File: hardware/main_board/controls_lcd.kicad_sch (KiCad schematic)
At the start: 28 parts, among them J3 2434804-1, Q1 AO3401A, Q3 AO3400A, Q4 AO3400A, Q5 AO3400A, SW3 SW_Push, U5 NHD-C0220BIZ-FSRGB

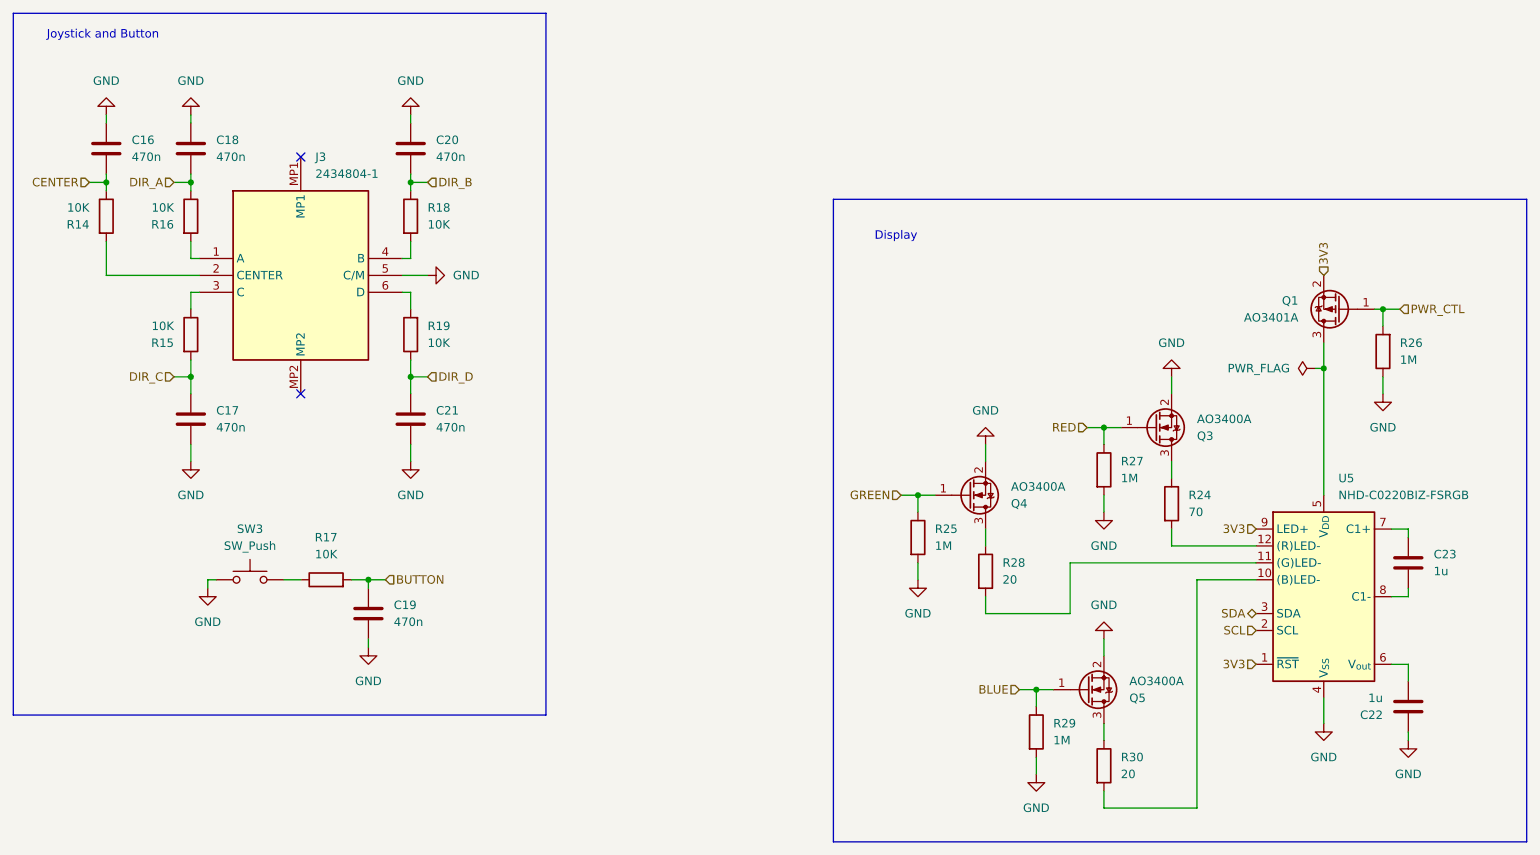
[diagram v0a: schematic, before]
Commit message: Add daughter board connector
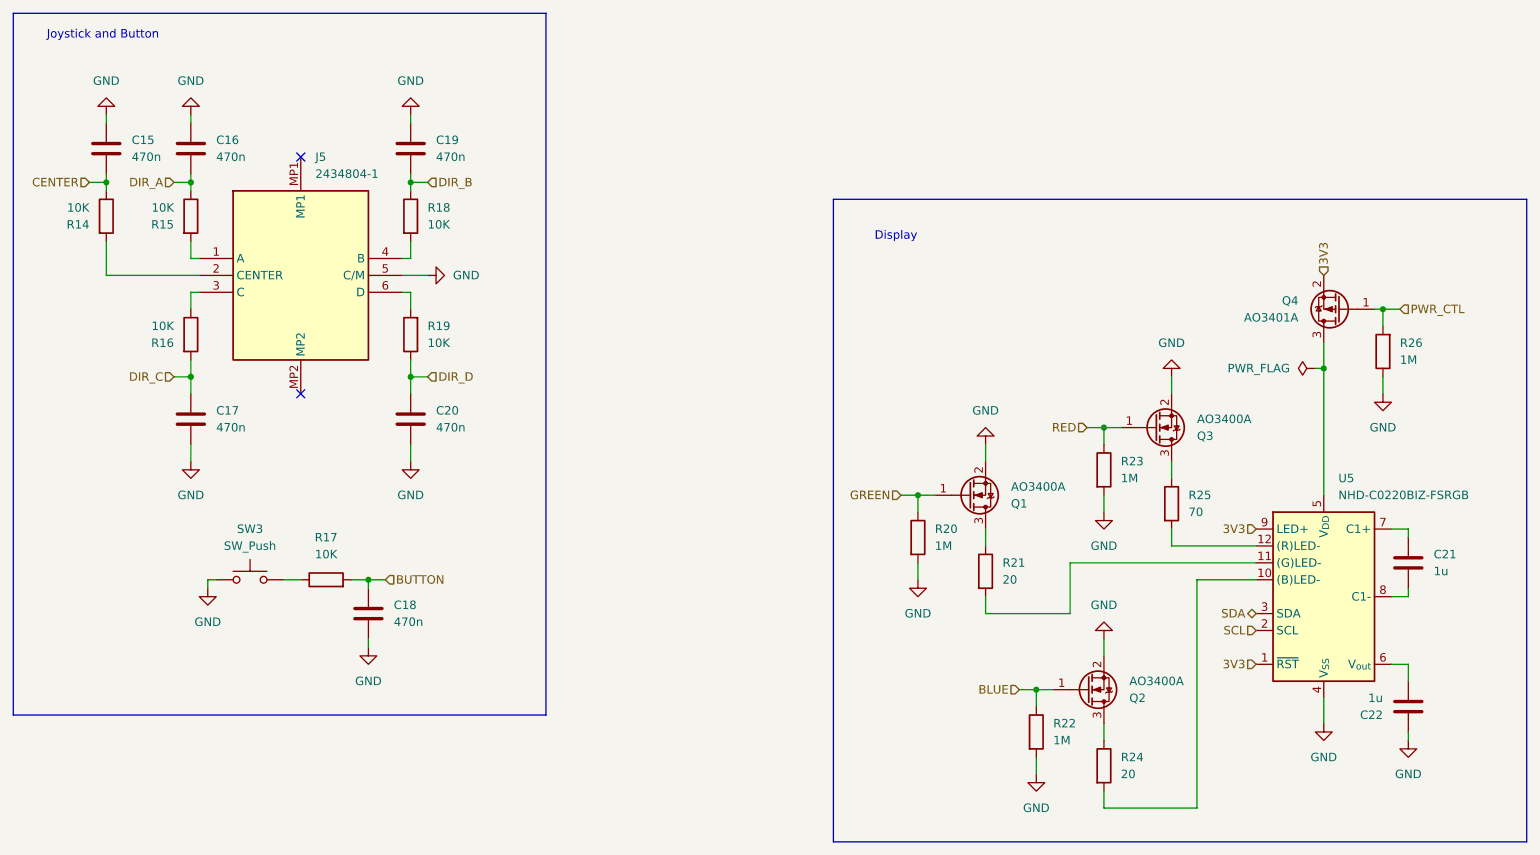
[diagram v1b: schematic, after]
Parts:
- J5: renamed from J3; footprint 24348041 -> Project_Footprints:TE_24348041
- renumbered C16 to C15, C18 to C16, C19 to C18, C20 to C19, C21 to C20, C23 to C21, Q4 to Q1, Q5 to Q2, Q1 to Q4, R16 to R15, R15 to R16, R25 to R20, R28 to R21, R29 to R22, R27 to R23, R30 to R24, R24 to R25

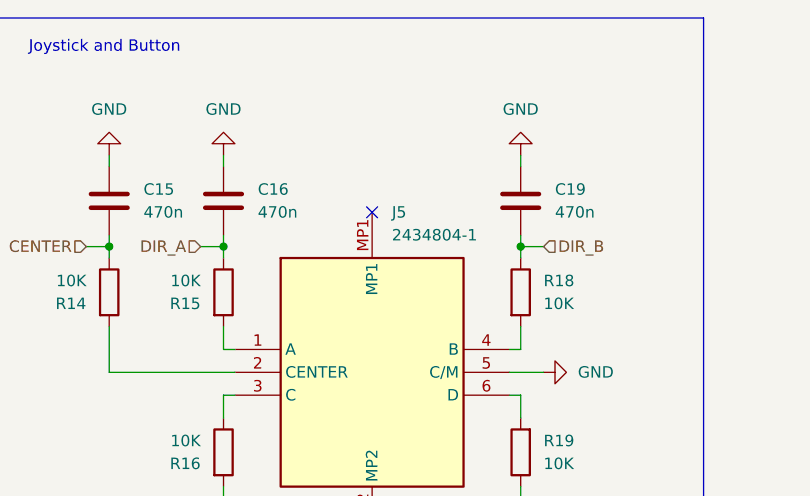
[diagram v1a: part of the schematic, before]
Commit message: Board schematic complete
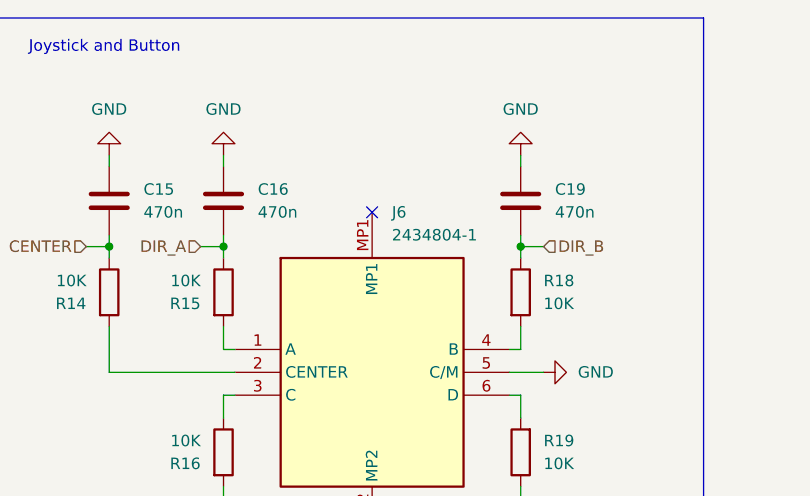
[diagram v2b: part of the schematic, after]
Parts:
- renumbered J5 to J6
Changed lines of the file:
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@@
 		(dnp no)
 		(fields_autoplaced yes)
-		(property "Reference" "#PWR033"
+		(property "Reference" "#PWR034"
 			(at 82.55 96.52 0)
 			(effects
@@
 			(project "main_board"
 				(path "/e7586151-38a0-41a9-9cce-542cfb7665db/8d2e8745-9bd7-47b1-9906-097dedd3973e"
-					(reference "#PWR033")
+					(reference "#PWR034")
 					(unit 1)
 				)
@@
 		(dnp no)
 		(fields_autoplaced yes)
-		(property "Reference" "#PWR037"
+		(property "Reference" "#PWR038"
 			(at 176.53 143.51 0)
 			(effects
@@
 			(project "main_board"
 				(path "/e7586151-38a0-41a9-9cce-542cfb7665db/8d2e8745-9bd7-47b1-9906-097dedd3973e"
-					(reference "#PWR037")
+					(reference "#PWR038")
 					(unit 1)
 				)
@@
 		(dnp no)
 		(fields_autoplaced yes)
-		(property "Reference" "#PWR043"
+		(property "Reference" "#PWR044"
 			(at 232.41 138.43 0)
 			(effects
@@
 			(project "main_board"
 				(path "/e7586151-38a0-41a9-9cce-542cfb7665db/8d2e8745-9bd7-47b1-9906-097dedd3973e"
-					(reference "#PWR043")
+					(reference "#PWR044")
 					(unit 1)
 				)
@@
 		(dnp no)
 		(fields_autoplaced yes)
-		(property "Reference" "#PWR040"
+		(property "Reference" "#PWR041"
 			(at 196.85 71.12 0)
 			(effects
@@
 			(project ""
 				(path "/e7586151-38a0-41a9-9cce-542cfb7665db/8d2e8745-9bd7-47b1-9906-097dedd3973e"
-					(reference "#PWR040")
+					(reference "#PWR041")
 					(unit 1)
 				)
@@
 		(dnp no)
 		(fields_autoplaced yes)
-		(property "Reference" "#PWR030"
+		(property "Reference" "#PWR031"
 			(at 52.07 115.57 0)
 			(effects
@@
 			(project "main_board"
 				(path "/e7586151-38a0-41a9-9cce-542cfb7665db/8d2e8745-9bd7-47b1-9906-097dedd3973e"
-					(reference "#PWR030")
+					(reference "#PWR031")
 					(unit 1)
 				)
@@
 		(dnp no)
 		(fields_autoplaced yes)
-		(property "Reference" "#PWR032"
+		(property "Reference" "#PWR033"
 			(at 82.55 31.75 0)
 			(effects
@@
 			(project ""
 				(path "/e7586151-38a0-41a9-9cce-542cfb7665db/8d2e8745-9bd7-47b1-9906-097dedd3973e"
-					(reference "#PWR032")
+					(reference "#PWR033")
 					(unit 1)
 				)
@@
 		(dnp no)
 		(fields_autoplaced yes)
-		(property "Reference" "#PWR035"
+		(property "Reference" "#PWR036"
 			(at 158.75 114.3 0)
 			(effects
@@
 			(project "main_board"
 				(path "/e7586151-38a0-41a9-9cce-542cfb7665db/8d2e8745-9bd7-47b1-9906-097dedd3973e"
-					(reference "#PWR035")
+					(reference "#PWR036")
 					(unit 1)
 				)
@@
 		(dnp no)
 		(fields_autoplaced yes)
-		(property "Reference" "#PWR039"
+		(property "Reference" "#PWR040"
 			(at 186.69 110.49 0)
 			(effects
@@
 			(project "main_board"
 				(path "/e7586151-38a0-41a9-9cce-542cfb7665db/8d2e8745-9bd7-47b1-9906-097dedd3973e"
-					(reference "#PWR039")
+					(reference "#PWR040")
 					(unit 1)
 				)
@@
 		(dnp no)
 		(fields_autoplaced yes)
-		(property "Reference" "#PWR042"
+		(property "Reference" "#PWR043"
 			(at 228.6 86.36 0)
 			(effects
@@
 			(project ""
 				(path "/e7586151-38a0-41a9-9cce-542cfb7665db/8d2e8745-9bd7-47b1-9906-097dedd3973e"
-					(reference "#PWR042")
+					(reference "#PWR043")
 					(unit 1)
 				)
@@
 		(dnp no)
 		(fields_autoplaced yes)
-		(property "Reference" "#PWR034"
+		(property "Reference" "#PWR035"
 			(at 91.44 62.23 0)
 			(effects
@@
 			(project "main_board"
 				(path "/e7586151-38a0-41a9-9cce-542cfb7665db/8d2e8745-9bd7-47b1-9906-097dedd3973e"
-					(reference "#PWR034")
+					(reference "#PWR035")
 					(unit 1)
 				)
@@
 		(dnp no)
 		(fields_autoplaced yes)
-		(property "Reference" "#PWR038"
+		(property "Reference" "#PWR039"
 			(at 186.69 104.14 0)
 			(effects
@@
 			(project ""
 				(path "/e7586151-38a0-41a9-9cce-542cfb7665db/8d2e8745-9bd7-47b1-9906-097dedd3973e"
-					(reference "#PWR038")
+					(reference "#PWR039")
 					(unit 1)
 				)
@@
 		(dnp no)
 		(fields_autoplaced yes)
-		(property "Reference" "#PWR027"
+		(property "Reference" "#PWR028"
 			(at 36.83 31.75 0)
 			(effects
@@
 			(project "main_board"
 				(path "/e7586151-38a0-41a9-9cce-542cfb7665db/8d2e8745-9bd7-47b1-9906-097dedd3973e"
-					(reference "#PWR027")
+					(reference "#PWR028")
 					(unit 1)
 				)
@@
 		(dnp no)
 		(fields_autoplaced yes)
-		(property "Reference" "#PWR028"
+		(property "Reference" "#PWR029"
 			(at 49.53 31.75 0)
 			(effects
@@
 			(project "main_board"
 				(path "/e7586151-38a0-41a9-9cce-542cfb7665db/8d2e8745-9bd7-47b1-9906-097dedd3973e"
-					(reference "#PWR028")
+					(reference "#PWR029")
 					(unit 1)
 				)
@@
 		(dnp no)
 		(fields_autoplaced yes)
-		(property "Reference" "J5"
+		(property "Reference" "J6"
 			(at 68.2341 44.45 0)
 			(effects
@@
 			(project ""
 				(path "/e7586151-38a0-41a9-9cce-542cfb7665db/8d2e8745-9bd7-47b1-9906-097dedd3973e"
-					(reference "J5")
+					(reference "J6")
 					(unit 1)
 				)
@@
 		(dnp no)
 		(fields_autoplaced yes)
-		(property "Reference" "#FLG03"
+		(property "Reference" "#FLG04"
 			(at 216.535 76.2 0)
 			(effects
@@
 			(project ""
 				(path "/e7586151-38a0-41a9-9cce-542cfb7665db/8d2e8745-9bd7-47b1-9906-097dedd3973e"
-					(reference "#FLG03")
+					(reference "#FLG04")
 					(unit 1)
 				)
@@
 		(dnp no)
 		(fields_autoplaced yes)
-		(property "Reference" "#PWR041"
+		(property "Reference" "#PWR042"
 			(at 219.71 135.89 0)
 			(effects
@@
 			(project "main_board"
 				(path "/e7586151-38a0-41a9-9cce-542cfb7665db/8d2e8745-9bd7-47b1-9906-097dedd3973e"
-					(reference "#PWR041")
+					(reference "#PWR042")
 					(unit 1)
 				)
@@
 		(dnp no)
 		(fields_autoplaced yes)
-		(property "Reference" "#PWR031"
+		(property "Reference" "#PWR032"
 			(at 76.2 124.46 0)
 			(effects
@@
 			(project "main_board"
 				(path "/e7586151-38a0-41a9-9cce-542cfb7665db/8d2e8745-9bd7-47b1-9906-097dedd3973e"
-					(reference "#PWR031")
+					(reference "#PWR032")
 					(unit 1)
 				)
@@
 		(dnp no)
 		(fields_autoplaced yes)
-		(property "Reference" "#PWR036"
+		(property "Reference" "#PWR037"
 			(at 168.91 81.28 0)
 			(effects
@@
 			(project "main_board"
 				(path "/e7586151-38a0-41a9-9cce-542cfb7665db/8d2e8745-9bd7-47b1-9906-097dedd3973e"
-					(reference "#PWR036")
+					(reference "#PWR037")
 					(unit 1)
 				)
@@
 		(dnp no)
 		(fields_autoplaced yes)
-		(property "Reference" "#PWR029"
+		(property "Reference" "#PWR030"
 			(at 49.53 96.52 0)
 			(effects
@@
 			(project "main_board"
 				(path "/e7586151-38a0-41a9-9cce-542cfb7665db/8d2e8745-9bd7-47b1-9906-097dedd3973e"
-					(reference "#PWR029")
+					(reference "#PWR030")
 					(unit 1)
 				)

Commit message: Routed mainboard PCB
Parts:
- R20, R22, R23: footprint (none) -> Resistor_SMD:R_0402_1005Metric
- U5: footprint Display:NHD-C0220BiZ-FSRGB -> Project_Footprints:NHD-C0220BiZ-FSRGB_no_mount
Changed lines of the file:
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@@
 			)
 		)
-		(property "Footprint" ""
+		(property "Footprint" "Resistor_SMD:R_0402_1005Metric"
 			(at 184.912 91.44 90)
 			(effects
@@
 		(dnp no)
 		(fields_autoplaced yes)
-		(property "Reference" "#PWR034"
+		(property "Reference" "#PWR35"
 			(at 82.55 96.52 0)
 			(effects
@@
 			(project "main_board"
 				(path "/e7586151-38a0-41a9-9cce-542cfb7665db/8d2e8745-9bd7-47b1-9906-097dedd3973e"
-					(reference "#PWR034")
+					(reference "#PWR35")
 					(unit 1)
 				)
@@
 		(dnp no)
 		(fields_autoplaced yes)
-		(property "Reference" "#PWR038"
+		(property "Reference" "#PWR39"
 			(at 176.53 143.51 0)
 			(effects
@@
 			(project "main_board"
 				(path "/e7586151-38a0-41a9-9cce-542cfb7665db/8d2e8745-9bd7-47b1-9906-097dedd3973e"
-					(reference "#PWR038")
+					(reference "#PWR39")
 					(unit 1)
 				)
@@
 		(dnp no)
 		(fields_autoplaced yes)
-		(property "Reference" "#PWR044"
+		(property "Reference" "#PWR45"
 			(at 232.41 138.43 0)
 			(effects
@@
 			(project "main_board"
 				(path "/e7586151-38a0-41a9-9cce-542cfb7665db/8d2e8745-9bd7-47b1-9906-097dedd3973e"
-					(reference "#PWR044")
+					(reference "#PWR45")
 					(unit 1)
 				)
@@
 			)
 		)
-		(property "Footprint" "Display:NHD-C0220BiZ-FSRGB"
+		(property "Footprint" "Project_Footprints:NHD-C0220BiZ-FSRGB_no_mount"
 			(at 219.71 113.03 0)
 			(effects
@@
 		(dnp no)
 		(fields_autoplaced yes)
-		(property "Reference" "#PWR041"
+		(property "Reference" "#PWR42"
 			(at 196.85 71.12 0)
 			(effects
@@
 			(project ""
 				(path "/e7586151-38a0-41a9-9cce-542cfb7665db/8d2e8745-9bd7-47b1-9906-097dedd3973e"
-					(reference "#PWR041")
+					(reference "#PWR42")
 					(unit 1)
 				)
@@
 			)
 		)
-		(property "Footprint" ""
+		(property "Footprint" "Resistor_SMD:R_0402_1005Metric"
 			(at 174.752 130.81 90)
 			(effects
@@
 		(dnp no)
 		(fields_autoplaced yes)
-		(property "Reference" "#PWR031"
+		(property "Reference" "#PWR32"
 			(at 52.07 115.57 0)
 			(effects
@@
 			(project "main_board"
 				(path "/e7586151-38a0-41a9-9cce-542cfb7665db/8d2e8745-9bd7-47b1-9906-097dedd3973e"
-					(reference "#PWR031")
+					(reference "#PWR32")
 					(unit 1)
 				)
@@
 			)
 		)
-		(property "Footprint" ""
+		(property "Footprint" "Resistor_SMD:R_0402_1005Metric"
 			(at 156.972 101.6 90)
 			(effects
@@
 		(dnp no)
 		(fields_autoplaced yes)
-		(property "Reference" "#PWR033"
+		(property "Reference" "#PWR34"
 			(at 82.55 31.75 0)
 			(effects
@@
 			(project ""
 				(path "/e7586151-38a0-41a9-9cce-542cfb7665db/8d2e8745-9bd7-47b1-9906-097dedd3973e"
-					(reference "#PWR033")
+					(reference "#PWR34")
 					(unit 1)
 				)
@@
 		(dnp no)
 		(fields_autoplaced yes)
-		(property "Reference" "#PWR036"
+		(property "Reference" "#PWR37"
 			(at 158.75 114.3 0)
 			(effects
@@
 			(project "main_board"
 				(path "/e7586151-38a0-41a9-9cce-542cfb7665db/8d2e8745-9bd7-47b1-9906-097dedd3973e"
-					(reference "#PWR036")
+					(reference "#PWR37")
 					(unit 1)
 				)
@@
 		(dnp no)
 		(fields_autoplaced yes)
-		(property "Reference" "#PWR040"
+		(property "Reference" "#PWR41"
 			(at 186.69 110.49 0)
 			(effects
@@
 			(project "main_board"
 				(path "/e7586151-38a0-41a9-9cce-542cfb7665db/8d2e8745-9bd7-47b1-9906-097dedd3973e"
-					(reference "#PWR040")
+					(reference "#PWR41")
 					(unit 1)
 				)
@@
 		(dnp no)
 		(fields_autoplaced yes)
-		(property "Reference" "#PWR043"
+		(property "Reference" "#PWR44"
 			(at 228.6 86.36 0)
 			(effects
@@
 			(project ""
 				(path "/e7586151-38a0-41a9-9cce-542cfb7665db/8d2e8745-9bd7-47b1-9906-097dedd3973e"
-					(reference "#PWR043")
+					(reference "#PWR44")
 					(unit 1)
 				)
@@
 		(dnp no)
 		(fields_autoplaced yes)
-		(property "Reference" "#PWR035"
+		(property "Reference" "#PWR36"
 			(at 91.44 62.23 0)
 			(effects
@@
 			(project "main_board"
 				(path "/e7586151-38a0-41a9-9cce-542cfb7665db/8d2e8745-9bd7-47b1-9906-097dedd3973e"
-					(reference "#PWR035")
+					(reference "#PWR36")
 					(unit 1)
 				)
@@
 		(dnp no)
 		(fields_autoplaced yes)
-		(property "Reference" "#PWR039"
+		(property "Reference" "#PWR40"
 			(at 186.69 104.14 0)
 			(effects
@@
 			(project ""
 				(path "/e7586151-38a0-41a9-9cce-542cfb7665db/8d2e8745-9bd7-47b1-9906-097dedd3973e"
-					(reference "#PWR039")
+					(reference "#PWR40")
 					(unit 1)
 				)
@@
 		(dnp no)
 		(fields_autoplaced yes)
-		(property "Reference" "#PWR028"
+		(property "Reference" "#PWR29"
 			(at 36.83 31.75 0)
 			(effects
@@
 			(project "main_board"
 				(path "/e7586151-38a0-41a9-9cce-542cfb7665db/8d2e8745-9bd7-47b1-9906-097dedd3973e"
-					(reference "#PWR028")
+					(reference "#PWR29")
 					(unit 1)
 				)
@@
 		(dnp no)
 		(fields_autoplaced yes)
-		(property "Reference" "#PWR029"
+		(property "Reference" "#PWR30"
 			(at 49.53 31.75 0)
 			(effects
@@
 			(project "main_board"
 				(path "/e7586151-38a0-41a9-9cce-542cfb7665db/8d2e8745-9bd7-47b1-9906-097dedd3973e"
-					(reference "#PWR029")
+					(reference "#PWR30")
 					(unit 1)
 				)
@@
 		(dnp no)
 		(fields_autoplaced yes)
-		(property "Reference" "#FLG04"
+		(property "Reference" "#FLG4"
 			(at 216.535 76.2 0)
 			(effects
@@
 			(project ""
 				(path "/e7586151-38a0-41a9-9cce-542cfb7665db/8d2e8745-9bd7-47b1-9906-097dedd3973e"
-					(reference "#FLG04")
+					(reference "#FLG4")
 					(unit 1)
 				)
@@
 		(dnp no)
 		(fields_autoplaced yes)
-		(property "Reference" "#PWR042"
+		(property "Reference" "#PWR43"
 			(at 219.71 135.89 0)
 			(effects
@@
 			(project "main_board"
 				(path "/e7586151-38a0-41a9-9cce-542cfb7665db/8d2e8745-9bd7-47b1-9906-097dedd3973e"
-					(reference "#PWR042")
+					(reference "#PWR43")
 					(unit 1)
 				)
@@
 		(dnp no)
 		(fields_autoplaced yes)
-		(property "Reference" "#PWR032"
+		(property "Reference" "#PWR33"
 			(at 76.2 124.46 0)
 			(effects
@@
 			(project "main_board"
 				(path "/e7586151-38a0-41a9-9cce-542cfb7665db/8d2e8745-9bd7-47b1-9906-097dedd3973e"
-					(reference "#PWR032")
+					(reference "#PWR33")
 					(unit 1)
 				)
@@
 		(dnp no)
 		(fields_autoplaced yes)
-		(property "Reference" "#PWR037"
+		(property "Reference" "#PWR38"
 			(at 168.91 81.28 0)
 			(effects
@@
 			(project "main_board"
 				(path "/e7586151-38a0-41a9-9cce-542cfb7665db/8d2e8745-9bd7-47b1-9906-097dedd3973e"
-					(reference "#PWR037")
+					(reference "#PWR38")
 					(unit 1)
 				)
@@
 		(dnp no)
 		(fields_autoplaced yes)
-		(property "Reference" "#PWR030"
+		(property "Reference" "#PWR31"
 			(at 49.53 96.52 0)
 			(effects
@@
 			(project "main_board"
 				(path "/e7586151-38a0-41a9-9cce-542cfb7665db/8d2e8745-9bd7-47b1-9906-097dedd3973e"
-					(reference "#PWR030")
+					(reference "#PWR31")
 					(unit 1)
 				)
